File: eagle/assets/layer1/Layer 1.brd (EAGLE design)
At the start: 196 x 185.3 mm, 248 parts, among them M1C1 33nF, M1C2 680uF, M1C3 1.0uF, M1D1 RED, M1D2 BLUE, M1J1 XT30PB-F, M1Q1 AOD482, M1R1 1k, M1R10 1k, M1R11 10k, M1R12 4.7k, M1R2 1k, M1R3 3.3k, M1R4 3.3k, M1R5 1k, M1R6 1k, M1R7 1k, M1R8 10k, M1R9 10k, M2C1 33nF, M2C2 680uF, M2C3 1.0uF, M2D1 RED, M2D2 BLUE, M2J1 XT30PB-F, M2Q1 AOD482, M2R1 1k, M2R10 1k, M2R11 10k, M2R12 4.7k, M2R2 1k, M2R3 3.3k, M2R4 3.3k, M2R5 1k, M2R6 1k, M2R7 1k, M2R8 10k, M2R9 10k, M3C1 33nF, M3C2 680uF, M3C3 1.0uF, M3D1 RED, M3D2 BLUE, M3J1 XT30PB-F, M3Q1 AOD482, M3R1 1k, M3R10 1k, M3R11 10k, M3R12 4.7k, M3R2 1k, M3R3 3.3k, M3R4 3.3k, M3R5 1k, M3R6 1k, M3R7 1k, M3R8 10k, M3R9 10k, M4C1 33nF, M4C2 680uF, M4C3 1.0uF, M4D1 RED, M4D2 BLUE, M4J1 XT30PB-F, M4Q1 AOD482, M4R1 1k, M4R10 1k, M4R11 10k, M4R12 4.7k, M4R2 1k, M4R3 3.3k, M4R4 3.3k, M4R5 1k, M4R6 1k, M4R7 1k, M4R8 10k, M4R9 10k, Q37 AO3402, X2 SM06B-SRSS-TB, Y1 8MHz

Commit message: Retarded eagle
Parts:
- moved R2 3.04 mm to (-83.0, 8.57)
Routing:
- net GND: track 218.4 -> 192.6 mm
- net RX1: track 123.6 -> 121.5 mm
- net N$70: track 4.13 -> 2.60 mm
- net BOOT0: track 104.1 -> 105.1 mm
- net LSWITCH: track 485.0 -> 485.8 mm
- net BL_PWM: track 47.9 -> 48.6 mm
- net TX1: track 127.3 -> 126.6 mm

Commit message: Final Check
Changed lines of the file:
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@@
 </layers>
 <board>
-<fusionsync huburn="a.YnVzaW5lc3M6Z21haWwxNDMxNzc3" projecturn="a.YnVzaW5lc3M6Z21haWwxNDMxNzc3IzIwMjIwMTE1NDg1NTYyMzgx" f3durn="urn:adsk.wipprod:dm.lineage:nDmFgUl6RZa3eTa8bgo8tA" pcbguid="" lastpulledtime="" lastsyncedchangeguid="" latestrevisionid="5e469cf1-c8af-4b5c-90f6-519c8d8b34f1" lastsyncedrevisionid="5e469cf1-c8af-4b5c-90f6-519c8d8b34f1" lastboardhashguid="7e7917c3-154f-edd2-a8ac-9bcbef2d575c" lastpushedtime="2022-02-21T13:39:18Z" linktopcb3d="true"/>
+<fusionsync huburn="a.YnVzaW5lc3M6Z21haWwxNDMxNzc3" projecturn="a.YnVzaW5lc3M6Z21haWwxNDMxNzc3IzIwMjIwMTE1NDg1NTYyMzgx" f3durn="urn:adsk.wipprod:dm.lineage:nDmFgUl6RZa3eTa8bgo8tA" pcbguid="" lastpulledtime="" lastsyncedchangeguid="" latestrevisionid="5e469cf1-c8af-4b5c-90f6-519c8d8b34f1" lastsyncedrevisionid="5e469cf1-c8af-4b5c-90f6-519c8d8b34f1" lastboardhashguid="7e7917c3-154f-edd2-a8ac-9bcbef2d575c" lastpushedtime="2022-02-21T13:39:18Z" linktopcb3d="false"/>
 <plain>
 <text x="-55.5" y="-9.2" size="0.6096" layer="25" rot="R90">3.3V</text>
@@
 <wire x1="5.42498125" y1="-7.824646875" x2="-0.19345" y2="-2.206215625" width="0.254" layer="16"/>
 <wire x1="-15.215890625" y1="-2.206215625" x2="-0.19345" y2="-2.206215625" width="0.254" layer="16"/>
-<via x="-40.27708125" y="-8.0422" extent="1-16" drill="0.508"/>
-<wire x1="-40.27708125" y1="-8.0422" x2="-39.6451875" y2="-7.41030625" width="0.254" layer="16"/>
-<wire x1="-39.6451875" y1="-7.41030625" x2="-20.41998125" y2="-7.41030625" width="0.254" layer="16"/>
-<wire x1="-40.27708125" y1="-8.0422" x2="-40.2683625" y2="-8.05091875" width="0.254" layer="1"/>
-<wire x1="-20.41998125" y1="-7.41030625" x2="-15.215890625" y2="-2.206215625" width="0.254" layer="16"/>
+<wire x1="-15.215890625" y1="-2.206215625" x2="-20.41998125" y2="-7.41030625" width="0.254" layer="16"/>
 <wire x1="-68.005303125" y1="-21.9642875" x2="-50.6175625" y2="-39.352028125" width="0.254" layer="1"/>
 <wire x1="-68" y1="-19.5" x2="-68.005303125" y2="-19.505303125" width="0.254" layer="1"/>
@@
 <via x="-42.768921875" y="-37.90804375" extent="1-16" drill="0.508"/>
 <wire x1="-42.768921875" y1="-37.90804375" x2="-42.768921875" y2="-26.044290625" width="0.254" layer="16"/>
-<wire x1="-42.768921875" y1="-26.044290625" x2="-40.261940625" y2="-23.537309375" width="0.254" layer="16"/>
-<via x="-40.291734375" y="-23.547240625" extent="1-16" drill="0.508"/>
-<wire x1="-40.291734375" y1="-23.547240625" x2="-40.291734375" y2="-8.056853125" width="0.254" layer="1"/>
-<wire x1="-40.291734375" y1="-8.056853125" x2="-40.27708125" y2="-8.0422" width="0.254" layer="1"/>
+<via x="-40.25863125" y="-23.596896875" extent="1-16" drill="0.508"/>
+<wire x1="-40.175871875" y1="-8.22196875" x2="-40.175871875" y2="-23.5141375" width="0.254" layer="1"/>
+<wire x1="-40.175871875" y1="-23.5141375" x2="-40.25863125" y2="-23.596896875" width="0.254" layer="1"/>
 <wire x1="-50.6175625" y1="-39.352028125" x2="-44.21290625" y2="-39.352028125" width="0.254" layer="1"/>
 <wire x1="-44.21290625" y1="-39.352028125" x2="-42.768921875" y2="-37.90804375" width="0.254" layer="1"/>
-<wire x1="-40.291734375" y1="-23.547240625" x2="-40.261940625" y2="-23.537309375" width="0" layer="19" extent="16-16"/>
+<wire x1="-42.768921875" y1="-26.044290625" x2="-40.321528125" y2="-23.596896875" width="0.2032" layer="16"/>
+<wire x1="-40.321528125" y1="-23.596896875" x2="-40.25863125" y2="-23.596896875" width="0.2032" layer="16"/>
+<via x="-40.35255625" y="-8.045284375" extent="1-16" drill="0.508"/>
+<wire x1="-40.35255625" y1="-8.045284375" x2="-40.175871875" y2="-8.22196875" width="0.254" layer="1"/>
+<wire x1="-39.717578125" y1="-7.41030625" x2="-40.35255625" y2="-8.045284375" width="0.254" layer="16"/>
+<wire x1="-20.41998125" y1="-7.41030625" x2="-39.717578125" y2="-7.41030625" width="0.254" layer="16"/>
 </signal>
 <signal name="TX3">

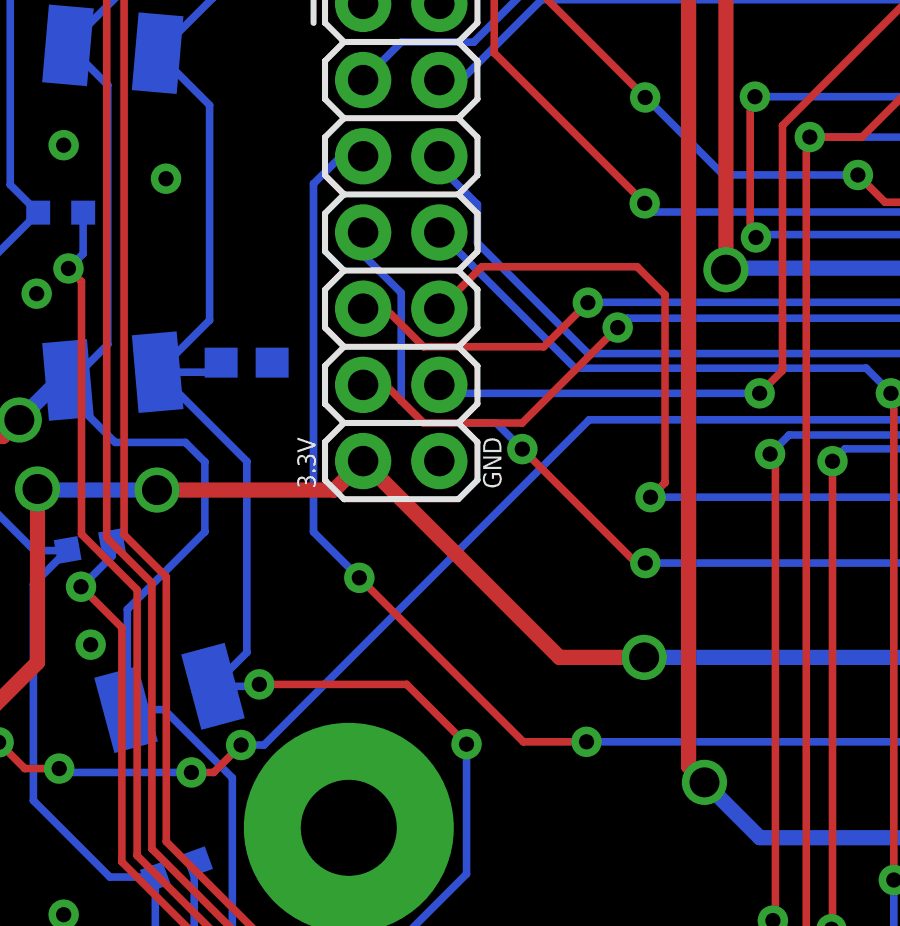
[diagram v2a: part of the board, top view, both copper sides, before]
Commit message: Added GND Connector
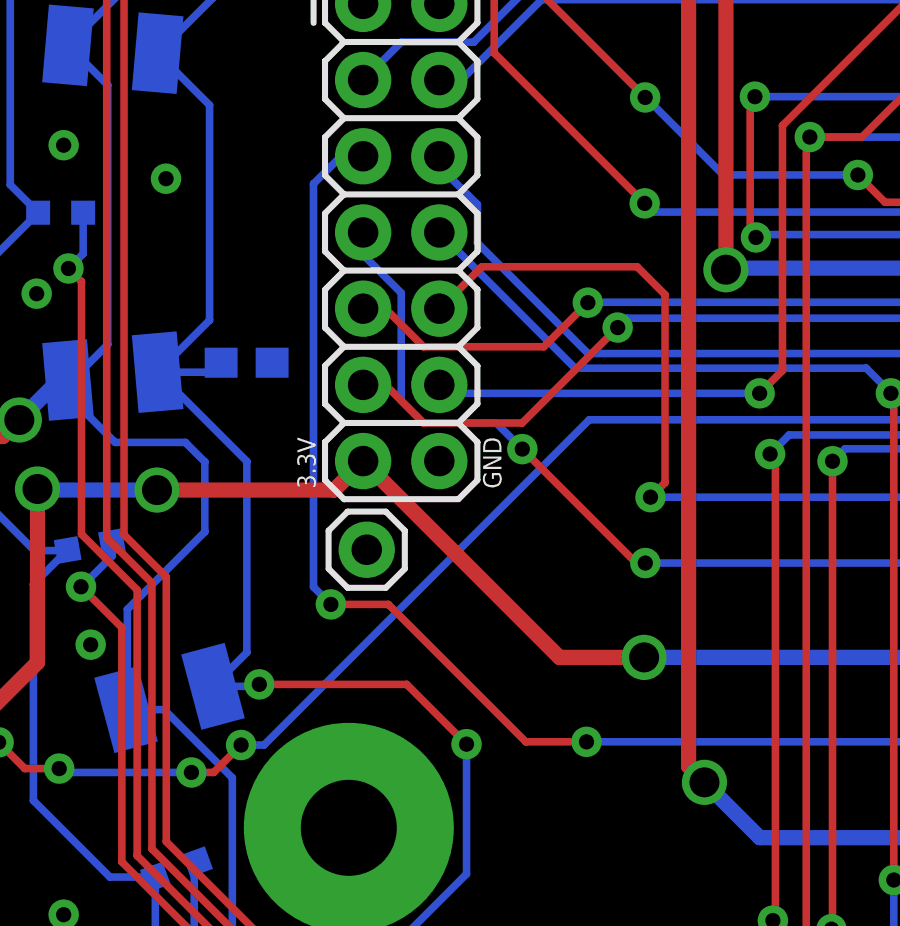
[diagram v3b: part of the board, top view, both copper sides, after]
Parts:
- added GND: (no value), SparkFun-Connectors:1X01
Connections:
- net GND: now also GND.1
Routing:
- net BL_DIR: track 78.9 -> 80.0 mm
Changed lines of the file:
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@@
 </layers>
 <board>
-<fusionsync huburn="a.YnVzaW5lc3M6Z21haWwxNDMxNzc3" projecturn="a.YnVzaW5lc3M6Z21haWwxNDMxNzc3IzIwMjIwMTE1NDg1NTYyMzgx" f3durn="urn:adsk.wipprod:dm.lineage:nDmFgUl6RZa3eTa8bgo8tA" pcbguid="" lastpulledtime="" lastsyncedchangeguid="" latestrevisionid="5e469cf1-c8af-4b5c-90f6-519c8d8b34f1" lastsyncedrevisionid="5e469cf1-c8af-4b5c-90f6-519c8d8b34f1" lastboardhashguid="7e7917c3-154f-edd2-a8ac-9bcbef2d575c" lastpushedtime="2022-02-21T13:39:18Z" linktopcb3d="false"/>
+<fusionsync huburn="a.YnVzaW5lc3M6Z21haWwxNDMxNzc3" projecturn="a.YnVzaW5lc3M6Z21haWwxNDMxNzc3IzIwMjIwMTE1NDg1NTYyMzgx" f3durn="urn:adsk.wipprod:dm.lineage:nDmFgUl6RZa3eTa8bgo8tA" pcbguid="" lastpulledtime="" lastsyncedchangeguid="" latestrevisionid="e85cee54-abec-4417-957b-6e46231fa4cb" lastsyncedrevisionid="e85cee54-abec-4417-957b-6e46231fa4cb" lastboardhashguid="0942933b-654a-1a33-018b-2fed2be7033b" lastpushedtime="2022-02-22T11:17:53Z" linktopcb3d="true"/>
 <plain>
 <text x="-55.5" y="-9.2" size="0.6096" layer="25" rot="R90">3.3V</text>
@@
 <attribute name="VALUE" x="-0.84201875" y="-50.565890625" size="0.7112" layer="27" font="vector" ratio="18" align="top-center"/>
 </element>
+<element name="GND" library="SparkFun-Connectors" library_urn="urn:adsk.eagle:library:513" package="1X01" package3d_urn="urn:adsk.eagle:package:38028/1" value="" x="-53.79758125" y="-11.2347375" smashed="yes">
+<attribute name="NAME" x="-55.314734375" y="-11.839696875" size="0.6096" layer="25" font="vector" ratio="20" rot="R90" display="off"/>
+<attribute name="VALUE" x="-55.06758125" y="-12.7587375" size="0.6096" layer="27" font="vector" ratio="20" align="top-left"/>
+</element>
 </elements>
 <signals>
@@
 <via x="60.32475" y="-8.21786875" extent="1-16" drill="0.508"/>
 <via x="-60.48860625" y="1.13275" extent="1-16" drill="0.508"/>
+<contactref element="GND" pad="1"/>
 </signal>
 <signal name="N$2">
@@
 <wire x1="-26.878984375" y1="-17.646984375" x2="-26.867671875" y2="-17.635671875" width="0.254" layer="1"/>
 <via x="-46.471840625" y="-17.63770625" extent="1-16" drill="0.508"/>
-<wire x1="-54.044584375" y1="-12.171446875" x2="-55.572725" y2="-10.64330625" width="0.254" layer="16"/>
-<wire x1="-55.572725" y1="-10.64330625" x2="-55.572725" y2="0.962596875" width="0.254" layer="16"/>
+<wire x1="-54.991971875" y1="-13.05705" x2="-55.572725" y2="-12.476296875" width="0.254" layer="16"/>
+<wire x1="-55.572725" y1="-12.476296875" x2="-55.572725" y2="0.962596875" width="0.254" layer="16"/>
 <wire x1="-55.572725" y1="0.962596875" x2="-54.654928125" y2="1.88039375" width="0.254" layer="16"/>
 <wire x1="-54.654928125" y1="1.88039375" x2="-53.918" y2="1.88039375" width="0.254" layer="16"/>
-<via x="-54.044584375" y="-12.171446875" extent="1-16" drill="0.508"/>
-<wire x1="-48.578325" y1="-17.63770625" x2="-54.044584375" y2="-12.171446875" width="0.254" layer="1"/>
-<wire x1="-46.471840625" y1="-17.63770625" x2="-48.578325" y2="-17.63770625" width="0.254" layer="1"/>
+<via x="-54.991971875" y="-13.05705" extent="1-16" drill="0.508"/>
+<wire x1="-48.495946875" y1="-17.63770625" x2="-53.076603125" y2="-13.05705" width="0.254" layer="1"/>
+<wire x1="-53.076603125" y1="-13.05705" x2="-54.991971875" y2="-13.05705" width="0.254" layer="1"/>
+<wire x1="-46.471840625" y1="-17.63770625" x2="-48.495946875" y2="-17.63770625" width="0.254" layer="1"/>
 </signal>
 <signal name="NOT_BL_DIR">

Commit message: Final PCB
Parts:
- moved X2 4.72 mm to (-70.0, -12.7)
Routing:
- net 3.3V: track 527.4 -> 520.6 mm
- net TX1: track 126.6 -> 132.1 mm
- net RX1: track 121.7 -> 126.8 mm
- net SWCLK: track 126.2 -> 131.2 mm
- net SWDIO: track 90.3 -> 94.0 mm

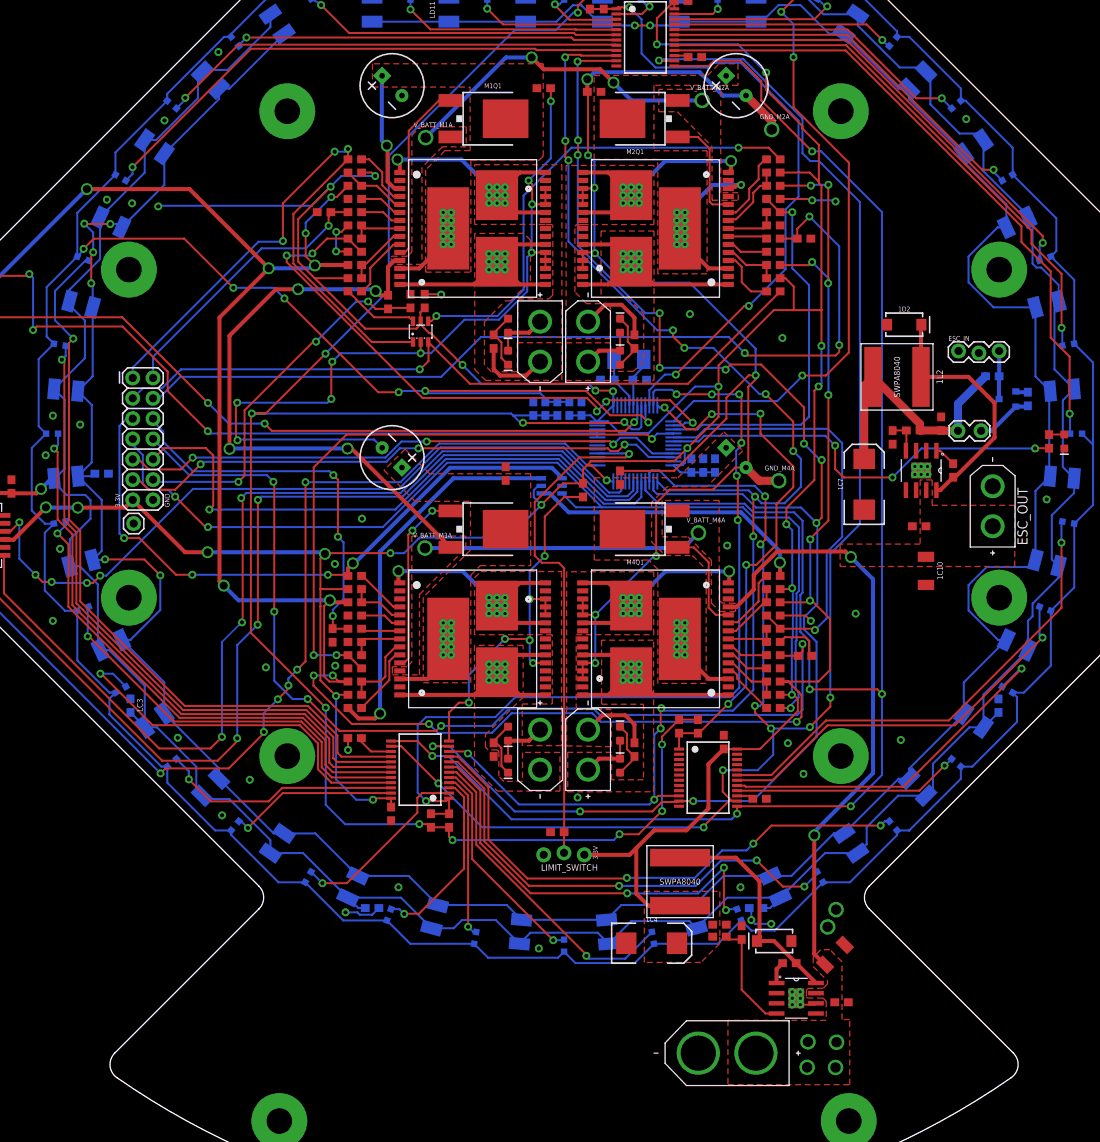
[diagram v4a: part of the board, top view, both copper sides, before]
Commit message: Made all the standoff vias GND
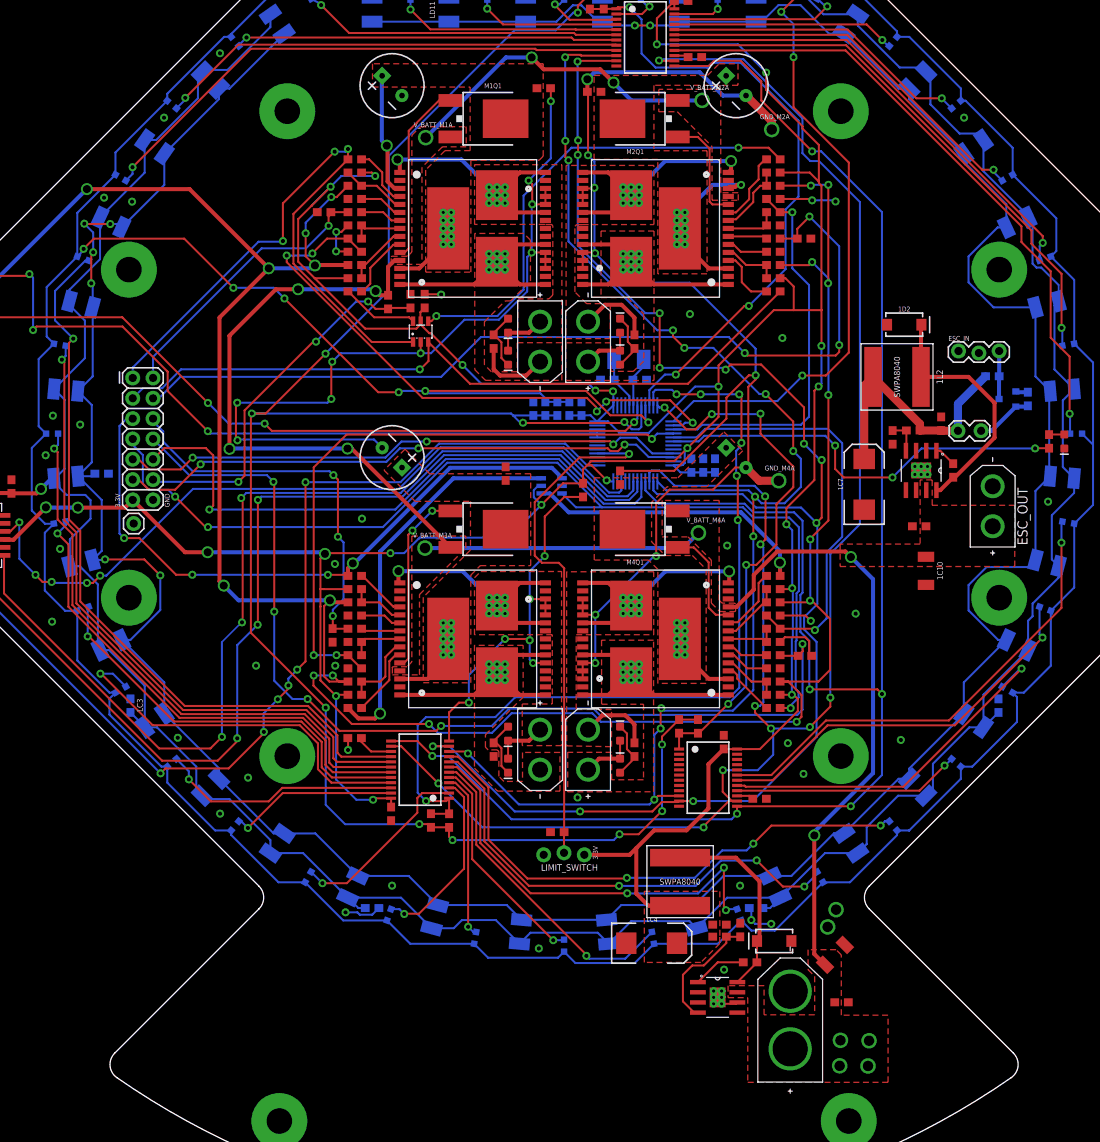
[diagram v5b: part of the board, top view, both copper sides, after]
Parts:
- moved U1 9.83 mm to (19.2, -70.5)
- moved U$1 8.90 mm to (28.3, -73.3), turned to 90 degrees
- moved 1C3 4.92 mm to (23.2, -66.1)
- moved V_BATT_M1B 4.07 mm to (38.1, -75.9)
- moved V_BATT_M2B 4.07 mm to (38.0, -79.0)
- moved V_BATT_M4B 4.07 mm to (34.5, -79.0)
- moved V_BATT_M3B 4.07 mm to (34.5, -75.8)
- moved 1R2 0.38 mm to (22.0, -62.0)
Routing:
- net 3.3V: track 520.6 -> 501.3 mm, vias 24 -> 23
- net N$1: track 2.80 -> 6.70 mm
- net N$2: track 28.3 -> 24.9 mm
- net N$4: track 13.9 -> 15.4 mm
- net GND: track 192.6 -> 191.6 mm, vias 54 -> 72

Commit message: Undid changes
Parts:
- moved GND_M4B 37.9 mm to (-4.00, -70.0)
- moved GND_M2B 31.8 mm to (4.00, -70.0)
- moved U1 6.90 mm to (17.3, -77.1)
- moved U$1 2.24 mm to (26.1, -72.9)
- moved V_BATT_M3B 1.76 mm to (33.0, -75.0)
- moved 1C3 1.58 mm to (21.8, -65.5)
- moved V_BATT_M4B 1.53 mm to (33.0, -79.5)
- moved V_BATT_M1B 0.89 mm to (38.0, -75.0)
- moved V_BATT_M2B 0.46 mm to (38.0, -79.5)
- moved 1R2 0.38 mm to (22.2, -62.4)
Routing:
- net N$4: track 15.4 -> 24.4 mm
- net N$2: track 24.9 -> 32.3 mm
- net N$1: track 6.70 -> 12.2 mm
- net 3.3V: track 501.3 -> 498.0 mm
- net GND: track 191.6 -> 194.6 mm, vias 72 -> 55
- net FL_DIR: track 78.5 -> 76.7 mm, vias 3 -> 1
